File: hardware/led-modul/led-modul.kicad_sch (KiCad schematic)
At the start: 0 parts

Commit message: Hardver: LED-modul kapcsolási rajz (vázlat) + generátor
6 low-side csatorna (NTD5C648NL, 3 × UCC27524, B360B szabadonfutó, RC snubber
DNP), blokkonként SMD biztosíték, ideális dióda (LM74700-Q1 + NTMFS5C604NL)
a 20 A-es ágon, gate- és drain-LED-ek, drain → ADC, 1 mΩ sönt + INA181A2,
NTC, MC78L12, HW-ID 2. sáv. DRV_EN-lehúzás 1 kΩ (D65). ERC: 0 hiba.

Co-Authored-By: Claude Opus 5.5 <noreply@anthropic.com>
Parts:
- added C201, C202, C207, C211, C213, C215, C240, C242: 100n, Capacitor_SMD:C_0603_1608Metric, symbol Device:C
- added C203: 470µ/50V, Capacitor_THT:CP_Radial_D10.0mm_P5.00mm, symbol Device:C_Polarized
- added C204, C205, C206: 10µ/50V, Capacitor_SMD:C_1210_3225Metric, symbol Device:C
- added C208: 1µ/50V, Capacitor_SMD:C_0805_2012Metric, symbol Device:C
- added C209: 10µ/25V, Capacitor_SMD:C_1206_3216Metric, symbol Device:C
- added C210, C212, C214: 1µ/25V, Capacitor_SMD:C_0805_2012Metric, symbol Device:C
- added C221, C222, C223, C224, C225, C226: 2n2/100V, Capacitor_SMD:C_1206_3216Metric, symbol Device:C
- added C231, C232, C233, C234, C235, C236: 10n, Capacitor_SMD:C_0603_1608Metric, symbol Device:C
- added C241: 1n, Capacitor_SMD:C_0603_1608Metric, symbol Device:C
- added D201: SMBJ28A, Diode_SMD:D_SMB, symbol Device:D_Zener
- added D211, D212, D213, D214, D215, D216: B360B, Diode_SMD:D_SMB, symbol Device:D_Schottky
- added D221, D222, D223, D224, D225, D226, D231, D232, D233, D234, D235, D236: zöld, LED_SMD:LED_0603_1608Metric, symbol Device:LED
- added F201: 20A, Fuse:Fuseholder_Blade_Mini_Keystone_3568, symbol Device:Fuse
- added F202, F203, F204: 10A, Fuse:Fuse_Littelfuse-NANO2-451_453, symbol Device:Fuse
- added J201: 24V IN 20A, TerminalBlock_Phoenix:TerminalBlock_Phoenix_MKDS-3-2-5.08_1x02_P5.08mm_Horizontal, symbol Connector_Generic:Conn_01x02
- added J202: BLOKK 1, TerminalBlock_Phoenix:TerminalBlock_Phoenix_MKDS-3-3-5.08_1x03_P5.08mm_Horizontal, symbol Connector_Generic:Conn_01x03
- added J203: BLOKK 2, TerminalBlock_Phoenix:TerminalBlock_Phoenix_MKDS-3-3-5.08_1x03_P5.08mm_Horizontal, symbol Connector_Generic:Conn_01x03
- added J204: BLOKK 3, TerminalBlock_Phoenix:TerminalBlock_Phoenix_MKDS-3-3-5.08_1x03_P5.08mm_Horizontal, symbol Connector_Generic:Conn_01x03
- added Q201: NTMFS5C604NL, Package_SO:ONSemi_SO-8FL_488AA, symbol Transistor_FET:NTMFS016N06CT1G
- added Q202, Q203, Q204, Q205, Q206, Q207: NTD5C648NL, Package_TO_SOT_SMD:TO-252-2, symbol Transistor_FET:QM6006D
- added R201, R208: 10k 1%, Resistor_SMD:R_0603_1608Metric, symbol Device:R
- added R202: 3k3 1%, Resistor_SMD:R_0603_1608Metric, symbol Device:R
- added R203: 100k, Resistor_SMD:R_0603_1608Metric, symbol Device:R
- added R204, R221, R222, R223, R224, R225, R226: 10k, Resistor_SMD:R_0603_1608Metric, symbol Device:R
- added R205: 1k, Resistor_SMD:R_0603_1608Metric, symbol Device:R
- added R207: 100R, Resistor_SMD:R_0603_1608Metric, symbol Device:R
- added R209: 1m 1%, Resistor_SMD:R_Shunt_Vishay_WSK2512_6332Metric_T1.19mm, symbol Device:R_Shunt
- added R211, R212, R213, R214, R215, R216: 10R, Resistor_SMD:R_0603_1608Metric, symbol Device:R
- added R231, R232, R233, R234, R235, R236: 10R, Resistor_SMD:R_1206_3216Metric, symbol Device:R
- added R241, R242, R243, R244, R245, R246: 4k7, Resistor_SMD:R_0603_1608Metric, symbol Device:R
- added R251, R252, R253, R254, R255, R256: 10k, Resistor_SMD:R_0805_2012Metric, symbol Device:R
- added R261, R262, R263, R264, R265, R266: 470k, Resistor_SMD:R_0603_1608Metric, symbol Device:R
- added R271, R272, R273, R274, R275, R276: 56k, Resistor_SMD:R_0603_1608Metric, symbol Device:R
- added TH201: 10k B3435, Resistor_SMD:R_0603_1608Metric, symbol Device:Thermistor_NTC
- added TP201: DAC_THR, TestPoint:TestPoint_Pad_D1.5mm, symbol Connector:TestPoint
- added TP202: I_SENSE, TestPoint:TestPoint_Pad_D1.5mm, symbol Connector:TestPoint
- added U201, U202, U203: UCC27524DR, Package_SO:SOIC-8_3.9x4.9mm_P1.27mm, symbol Driver_FET:UCC27524D
- added U204: LM74700-Q1, Package_TO_SOT_SMD:SOT-23-6, symbol Power_Management:LM74700
- added U205: MC78L12ACDR2G, Package_SO:SOIC-8_3.9x4.9mm_P1.27mm, symbol Regulator_Linear:MC78L12_SO8
- added U206: INA181A2IDBVR, Package_TO_SOT_SMD:SOT-23-6, symbol Amplifier_Current:INA181
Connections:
- new net +12V: C209.1, C210.1, C211.1, C212.1, C213.1, C214.1, C215.1, U201.6 (V_{DD}), U202.6 (V_{DD}), U203.6 (V_{DD}), U205.1 (OUT)
- new net +24V_B1: D211.1 (K), D212.1 (K), F202.2, J202.1 (Pin_1), R251.1, R252.1
- new net +24V_B2: D213.1 (K), D214.1 (K), F203.2, J203.1 (Pin_1), R253.1, R254.1
- new net +24V_B3: D215.1 (K), D216.1 (K), F204.2, J204.1 (Pin_1), R255.1, R256.1
- new net +24V_F: C202.2, F201.2, Q201.1 (S), Q201.2 (S), Q201.3 (S), U204.3 (EN), U204.6 (ANODE)
- new net +24V_IN: F201.1, J201.1 (Pin_1)
- new net +24V_RAIL: C203.1, C204.1, C205.1, C206.1, C208.1, D201.1 (K), F202.1, F203.1, F204.1, Q201.5 (D), R203.1, U204.4 (CATHODE), U205.8 (IN)
- new net +3V3: C240.1, R201.1, R208.1, U206.6 (V+)
- new net CH1_D: D211.2 (A), D231.1 (K), J202.2 (Pin_2), Q202.2 (D), R231.1, R261.1
- new net CH1_G: Q202.1 (G), R211.2, R221.1
- new net CH1_GD: R211.1, R241.1, U201.7 (OUTA)
- new net CH1_PWM: U201.2 (INA)
- new net CH1_SN: C221.1, R231.2
- new net CH2_D: D212.2 (A), D232.1 (K), J202.3 (Pin_3), Q203.2 (D), R232.1, R262.1
- new net CH2_G: Q203.1 (G), R212.2, R222.1
- new net CH2_GD: R212.1, R242.1, U201.5 (OUTB)
- new net CH2_PWM: U201.4 (INB)
- new net CH2_SN: C222.1, R232.2
- new net CH3_D: D213.2 (A), D233.1 (K), J203.2 (Pin_2), Q204.2 (D), R233.1, R263.1
- new net CH3_G: Q204.1 (G), R213.2, R223.1
- new net CH3_GD: R213.1, R243.1, U202.7 (OUTA)
- new net CH3_PWM: U202.2 (INA)
- new net CH3_SN: C223.1, R233.2
- new net CH4_D: D214.2 (A), D234.1 (K), J203.3 (Pin_3), Q205.2 (D), R234.1, R264.1
- new net CH4_G: Q205.1 (G), R214.2, R224.1
- new net CH4_GD: R214.1, R244.1, U202.5 (OUTB)
- new net CH4_PWM: U202.4 (INB)
- new net CH4_SN: C224.1, R234.2
- new net CH5_D: D215.2 (A), D235.1 (K), J204.2 (Pin_2), Q206.2 (D), R235.1, R265.1
- new net CH5_G: Q206.1 (G), R215.2, R225.1
- new net CH5_GD: R215.1, R245.1, U203.7 (OUTA)
- new net CH5_PWM: U203.2 (INA)
- new net CH5_SN: C225.1, R235.2
- new net CH6_D: D216.2 (A), D236.1 (K), J204.3 (Pin_3), Q207.2 (D), R236.1, R266.1
- new net CH6_G: Q207.1 (G), R216.2, R226.1
- new net CH6_GD: R216.1, R246.1, U203.5 (OUTB)
- new net CH6_PWM: U203.4 (INB)
- new net CH6_SN: C226.1, R236.2
- new net DAC_THR: TP201.1
- new net DLED1: D231.2 (A), R251.2
- new net DLED2: D232.2 (A), R252.2
- new net DLED3: D233.2 (A), R253.2
- new net DLED4: D234.2 (A), R254.2
- new net DLED5: D235.2 (A), R255.2
- new net DLED6: D236.2 (A), R256.2
- new net DRV_EN: R205.1, U201.1 (ENA), U201.8 (ENB), U202.1 (ENA), U202.8 (ENB), U203.1 (ENA), U203.8 (ENB)
- new net DS1: C231.1, R261.2, R271.1
- new net DS2: C232.1, R262.2, R272.1
- new net DS3: C233.1, R263.2, R273.1
- new net DS4: C234.1, R264.2, R274.1
- new net DS5: C235.1, R265.2, R275.1
- new net DS6: C236.1, R266.2, R276.1
- new net GLED1: D221.2 (A), R241.2
- new net GLED2: D222.2 (A), R242.2
- new net GLED3: D223.2 (A), R243.2
- new net GLED4: D224.2 (A), R244.2
- new net GLED5: D225.2 (A), R245.2
- new net GLED6: D226.2 (A), R246.2
- new net GND: C201.2, C203.2, C204.2, C205.2, C206.2, C207.2, C208.2, C209.2, C210.2, C211.2, C212.2, C213.2, C214.2, C215.2, C231.2, C232.2, C233.2, C234.2, C235.2, C236.2, C240.2, C241.2, C242.2, D201.2 (A), D221.1 (K), D222.1 (K), D223.1 (K), D224.1 (K), D225.1 (K), D226.1 (K), J201.2 (Pin_2), R202.2, R204.2, R205.2, R209.4, R271.2, R272.2, R273.2, R274.2, R275.2, R276.2, TH201.2, U201.3 (GND), U202.3 (GND), U203.3 (GND), U204.2 (GND), U205.2 (GND), U205.3 (GND), U205.6 (GND), U205.7 (GND), U206.2 (GND), U206.5 (REF)
- new net HW_ID: C201.1, R201.2, R202.1
- new net IDEAL_GATE: Q201.4 (G), U204.5 (GATE)
- new net IDEAL_VCAP: C202.1, U204.1 (VCAP)
- new net INA_OUT: R207.1, U206.1
- new net ISNS_N: R209.3, U206.4 (-)
- new net ISNS_P: R209.2, U206.3 (+)
- new net I_SENSE: C241.1, R207.2, TP202.1
- new net NTC: C242.1, R208.2, TH201.1
- new net PGND_SH: C221.2, C222.2, C223.2, C224.2, C225.2, C226.2, Q202.3 (S), Q203.3 (S), Q204.3 (S), Q205.3 (S), Q206.3 (S), Q207.3 (S), R209.1, R221.2, R222.2, R223.2, R224.2, R225.2, R226.2
- new net V_RAIL_SENSE: C207.1, R203.2, R204.1
- no-connect marks 0 -> 10
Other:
- added sheet modulmag (../modulmag/modulmag.kicad_sch)
- note added: "1 mΩ sönt: PGND_SH (FET-source-ok) → GND, Kelvin"
- note added: "1. BETÁP (20 A): J201 → F201 20 A (mini lapos) → ideális dióda (U204 LM74700-Q1 + Q201) → +24V_RAIL"
- note added: "2. KIMENETI BLOKKOK: [+24 V, CHa, CHb] × 3, blokkonként SMD biztosíték (D65) – a szalagok közös vezetéke a +24 V (low-side, D43)"
- note added: "3. GATE-MEGHAJTÓK – 3 × UCC27524 (12 V): EN közösen a DRV_EN-en (PB12), 1 k lehúzás → bekapcsoláskor minden csatorna KI"
- note added: "4. CSATORNÁK (× 6): FET NTD5C648NL (DPAK; tartalék IRFR1205) · szabadonfutó B360B a blokk +24 V-jára · RC snubber (DNP)"
- note added: "5. ÖSSZ-ÁRAM (D47, D53)"
- note added: "6 EN-láb belső 200 k felhúzása a 12 V-ra párhuzamosan ~33 k → 1 k-val ~0,35 V (< 0,8 V); az IN-lábakon 120 k belső lehúzás is van"
- note added: "BE: ≈ V_RAIL × (1 − kitöltés); mindig ~0 V = átütött FET. A „nincs szalag” biztosan az önteszt áramméréséből (D47) látszik."
- note added: "Drain → ADC: 24 V → 2,55 V (PA0–PA3, PA5, PA6). KI: ≈ V_RAIL = szalag rajta; ≈ V_RAIL − ~2 V = nincs szalag (a drain-LED-en át, halványan dereng); ~0 V = kiolvadt blokk-biztosíték"
- note added: "HW-ID: LED-modul = 2. sáv (0,82 V)"
- note added: "INA181A2 (×50) → PA7: ADC + COMP2 → TIM1/TIM8 break"
- note added: "MODULMAG – a logikai táp a 20 A-es"
- note added: "NTC a FET-ek között (PC3)"
- note added: "V_RAIL: 24 V → 2,2 V (PC2); a VIN_SENSE-szel (PC1)"
- note added: "VÁZLAT – generálva a MODULMAG-SPEC + D43/D47/D53/D65 alapján (2026-10-14). Elrendezést rendezd; a bekötés címkékkel kész."
- note added: "együtt a kiégett F201 / hibás Q201 jelezhető"
- note added: "fordított polaritás ellen, GND-eltolódás nélkül (D65); Q201 hiányában S–D dróttal áthidalható"
- note added: "főbiztosíték ELŐTT ágazik le (D54)"
- note added: "gate-LED (driver kimenet) + drain-LED (a blokk +24 V-ja → drain) · drain → ADC osztó (D65)"
- note added: "küszöb: DAC1 (PA4); 20 A → 1,0 V"
- title: LED-modul (6 csatorna) -> LED-modul – 6 × 10 A low-side PWM (össz. 20 A), modulmag

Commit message: Hardver: mind az öt kapcsolási rajz elrendezve (vezetékes, blokkos), netlista-ellenőrzővel
Funkcionális blokkok, balról jobbra jelút, tápsín felül / GND alul; blokkon belül
vezeték, blokkok között és az IC-lábakon címke. kigen: lábpozíció, place(),
wire/junction/rail, tükrözés, 1,27 mm-es rács, olvasható mezők. gen/netcmp.py:
két netlista lábszintű összevetése – a bekötés az átrendezés előttivel azonos
(a modulmag D66-os D6/JP2-jét kivéve). ERC: 0 hiba mind az öt lapon.

Co-Authored-By: Claude Opus 5.5 <noreply@anthropic.com>
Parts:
- C203: Megjegyzés low-ESR, 105 °C; a GND-oldala a sönt ELŐTT (a sönt a FET-ár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 -> low-ESR, 105 °C; GND-oldala a sönt ELŐTT
- C204, C205, C206: Megjegyzés a FET-ek mellett, csatornapáronként egy -> a FET-ek mellett
- D201: Megjegyzés TVS a sínen – a P78E05-ös logikai ágon a modulmag D2-je véd -> TVS a sínen
- J201: Megjegyzés push-in, 2,5 mm², ≥ 20 A – helyőrző, a DIN-ház szerint; bar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 -> push-in, 2,5 mm², ≥ 20 A – helyőrző; barna = +24 V, kék = G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
- Q201: Megjegyzés onsemi 60 V, ~1,2 mΩ, SO-8FL; S = bemenet, D = sín. Nagy pa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 -> onsemi 60 V, ~1,2 mΩ, SO-8FL; S = bemenet, D = sín; nagy pa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
- TH201: Megjegyzés a FET-ek között, a NYÁK-on (D30 – harmadik védelmi réteg) -> (none)
- U204: Megjegyzés TI ideális dióda-vezérlő; EN az ANODE-ra (mindig BE) -> TI ideális dióda-vezérlő; EN az ANODE-ra
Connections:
- net CH1_G: no longer names the net of Q202.1 (G), R211.2, R221.1
- net CH1_SN: no longer names the net of C221.1, R231.2
- net CH2_G: no longer names the net of Q203.1 (G), R212.2, R222.1
- net CH2_SN: no longer names the net of C222.1, R232.2
- net CH3_G: no longer names the net of Q204.1 (G), R213.2, R223.1
- net CH3_SN: no longer names the net of C223.1, R233.2
- net CH4_G: no longer names the net of Q205.1 (G), R214.2, R224.1
- net CH4_SN: no longer names the net of C224.1, R234.2
- net CH5_G: no longer names the net of Q206.1 (G), R215.2, R225.1
- net CH5_SN: no longer names the net of C225.1, R235.2
- net CH6_G: no longer names the net of Q207.1 (G), R216.2, R226.1
- net CH6_SN: no longer names the net of C226.1, R236.2
- net DLED1: no longer names the net of D231.2 (A), R251.2
- net DLED2: no longer names the net of D232.2 (A), R252.2
- net DLED3: no longer names the net of D233.2 (A), R253.2
- net DLED4: no longer names the net of D234.2 (A), R254.2
- net DLED5: no longer names the net of D235.2 (A), R255.2
- net DLED6: no longer names the net of D236.2 (A), R256.2
- net GLED1: no longer names the net of D221.2 (A), R241.2
- net GLED2: no longer names the net of D222.2 (A), R242.2
- net GLED3: no longer names the net of D223.2 (A), R243.2
- net GLED4: no longer names the net of D224.2 (A), R244.2
- net GLED5: no longer names the net of D225.2 (A), R245.2
- net GLED6: no longer names the net of D226.2 (A), R246.2
- net IDEAL_GATE: no longer names the net of Q201.4 (G), U204.5 (GATE)
- net IDEAL_VCAP: no longer names the net of C202.1, U204.1 (VCAP)
- net INA_OUT: no longer names the net of R207.1, U206.1
- net ISNS_N: no longer names the net of R209.3, U206.4 (-)
- net ISNS_P: no longer names the net of R209.2, U206.3 (+)
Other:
- note added: "(ADC + COMP2 → TIM1/TIM8 break); a küszöb a DAC1-ről (PA4); 20 A → 1,0 V"
- note added: "1. BETÁP (20 A): J201 → F201 20 A → ideális dióda (U204 LM74700-Q1 + Q201) → +24V_RAIL – fordított polaritás ellen, GND-eltolódás nélkül (D65)"
- note added: "2. GATE-MEGHAJTÓK – 3 × UCC27524 (12 V): EN közösen a DRV_EN-en (PB12), 1 k lehúzás → bekapcsoláskor minden csatorna KI"
- note added: "3. CSATORNÁK (× 6): FET NTD5C648NL (DPAK; tartalék IRFR1205) · szabadonfutó B360B a blokk +24 V-jára · RC snubber (DNP) · gate-LED + drain-LED · drain → ADC osztó"
- note added: "4. ÖSSZ-ÁRAM (D47, D53): 1 mΩ sönt a FET-ek közös source-ága (PGND_SH) és a GND között, Kelvin → INA181A2 (×50) → PA7"
- note added: "CH1"
- note added: "CH2"
- note added: "CH3"
- note added: "CH4"
- note added: "CH5"
- note added: "CH6"
- note added: "Drain → ADC: 24 V → 2,55 V. KI: ≈ V_RAIL = szalag rajta; ≈ V_RAIL − ~2 V = nincs szalag (a drain-LED-en át); ~0 V = kiolvadt blokk-biztosíték. BE: ≈ V_RAIL × (1 − kitöltés); mindig ~0 V = átütött FET"
- note added: "Generálva (hardware/gen/led-modul.py) – D43/D47/D53/D65 alapján; kézi szerkesztés helyett a generátort módosítsd."
- note added: "NTC a FET-ek között (PC3) – D30, harmadik védelmi réteg"
- note added: "Q201 hiányában a S–D padek vastag dróttal áthidalhatók"
- note added: "V_RAIL → PC2"
- note added: "pufferek: a GND-oldaluk a sönt előtt"
- note removed: "1 mΩ sönt: PGND_SH (FET-source-ok) → GND, Kelvin"
- note removed: "1. BETÁP (20 A): J201 → F201 20 A (mini lapos) → ideális dióda (U204 LM74700-Q1 + Q201) → +24V_RAIL"
- note removed: "2. KIMENETI BLOKKOK: [+24 V, CHa, CHb] × 3, blokkonként SMD biztosíték (D65) – a szalagok közös vezetéke a +24 V (low-side, D43)"
- note removed: "3. GATE-MEGHAJTÓK – 3 × UCC27524 (12 V): EN közösen a DRV_EN-en (PB12), 1 k lehúzás → bekapcsoláskor minden csatorna KI"
- note removed: "4. CSATORNÁK (× 6): FET NTD5C648NL (DPAK; tartalék IRFR1205) · szabadonfutó B360B a blokk +24 V-jára · RC snubber (DNP)"
- note removed: "5. ÖSSZ-ÁRAM (D47, D53)"
- note removed: "BE: ≈ V_RAIL × (1 − kitöltés); mindig ~0 V = átütött FET. A „nincs szalag” biztosan az önteszt áramméréséből (D47) látszik."
- note removed: "Drain → ADC: 24 V → 2,55 V (PA0–PA3, PA5, PA6). KI: ≈ V_RAIL = szalag rajta; ≈ V_RAIL − ~2 V = nincs szalag (a drain-LED-en át, halványan dereng); ~0 V = kiolvadt blokk-biztosíték"
- note removed: "INA181A2 (×50) → PA7: ADC + COMP2 → TIM1/TIM8 break"
- note removed: "NTC a FET-ek között (PC3)"
- note removed: "V_RAIL: 24 V → 2,2 V (PC2); a VIN_SENSE-szel (PC1)"
- note removed: "VÁZLAT – generálva a MODULMAG-SPEC + D43/D47/D53/D65 alapján (2026-10-14). Elrendezést rendezd; a bekötés címkékkel kész."
- note removed: "együtt a kiégett F201 / hibás Q201 jelezhető"
- note removed: "fordított polaritás ellen, GND-eltolódás nélkül (D65); Q201 hiányában S–D dróttal áthidalható"
- note removed: "gate-LED (driver kimenet) + drain-LED (a blokk +24 V-ja → drain) · drain → ADC osztó (D65)"
- note removed: "küszöb: DAC1 (PA4); 20 A → 1,0 V"

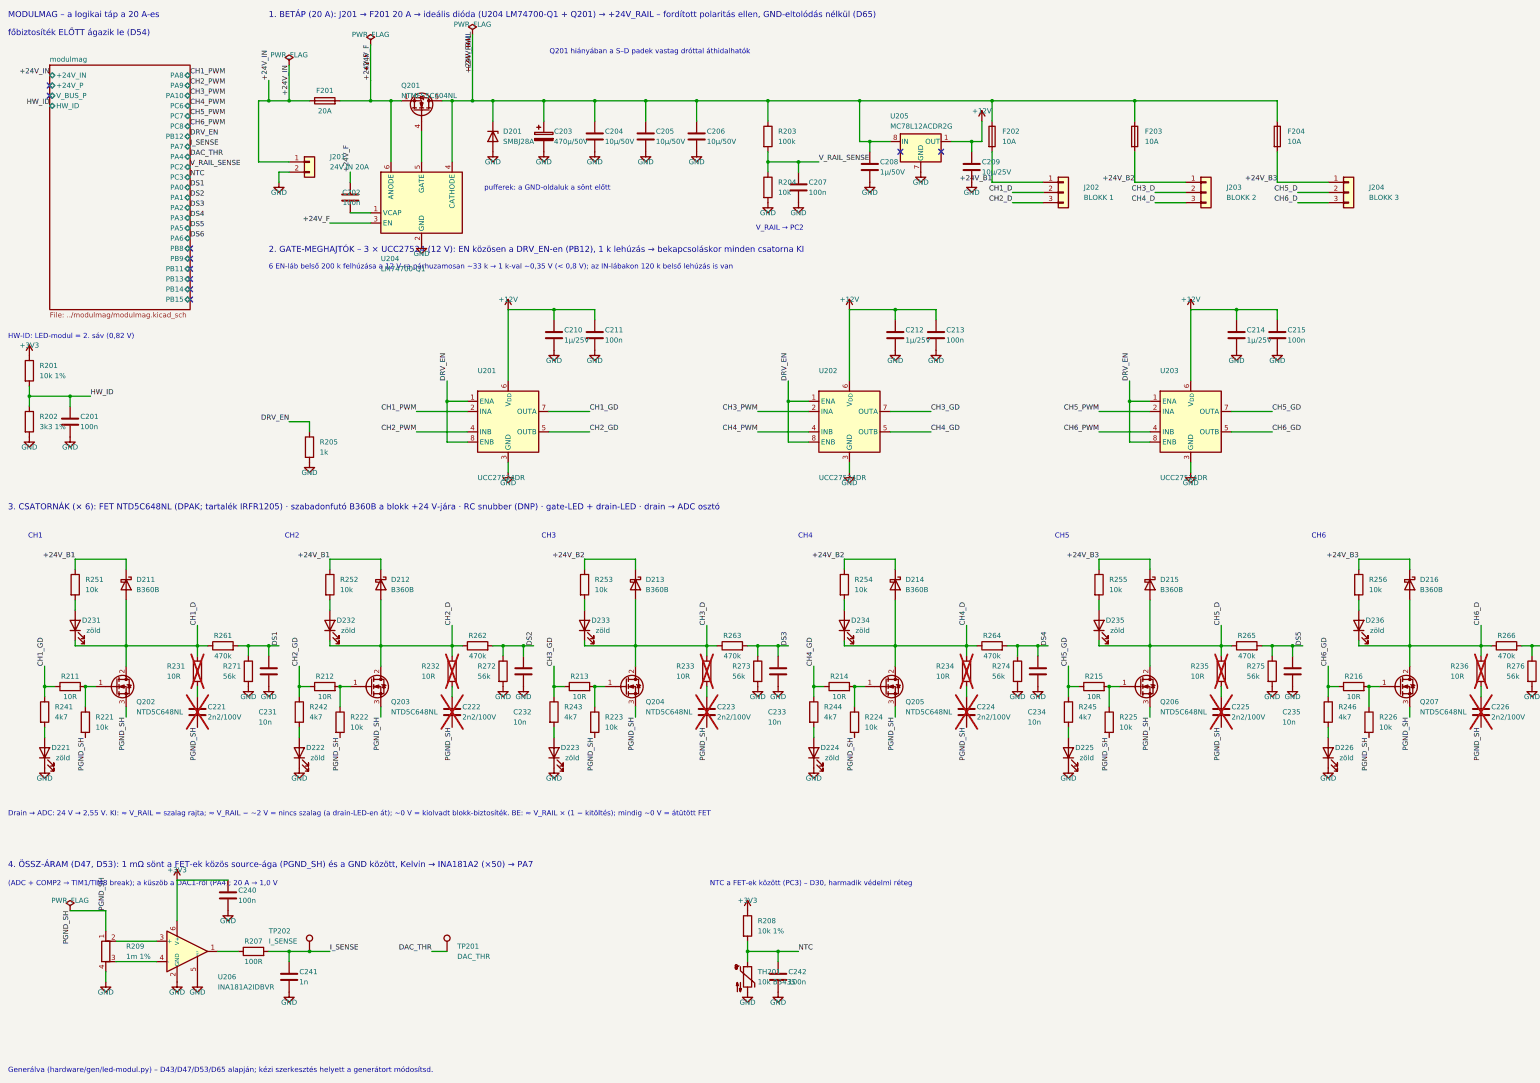
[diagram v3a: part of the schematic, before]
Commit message: Hardver: átnézés (C320 javítva), LoRa-előkészítés (D68), bővítők (D69), R6/R7 = 0 Ω (D70)
- bemeneti modul: a HDC3020 hidegítője C330 lett (a C320 kétszer szerepelt);
  a generátor mostantól hibát dob duplikált jelölésre
- vezérlő: E22-900M22S LoRa + u.FL + 74LVC1G04, minden DNP; J8 bővítő (GPIO5),
  7 mérőpont; spec szerinti DNP-k (USB C, 1 MΩ, PMODE, CAN-fojtó + áthidalók);
  saját footprint az LMR36015-höz (RNX) és az E22-höz
- modulmag: HW_REV osztó (PB0), DNP J4 2 × 5 bővítő; relé: DNP SCT-013 → PA0
- mind az öt lap vizuálisan rendbe téve; R6/R7 = 0 Ω
- specek és döntésnapló frissítve (D68–D70)

Co-Authored-By: Claude Opus 5.5 <noreply@anthropic.com>
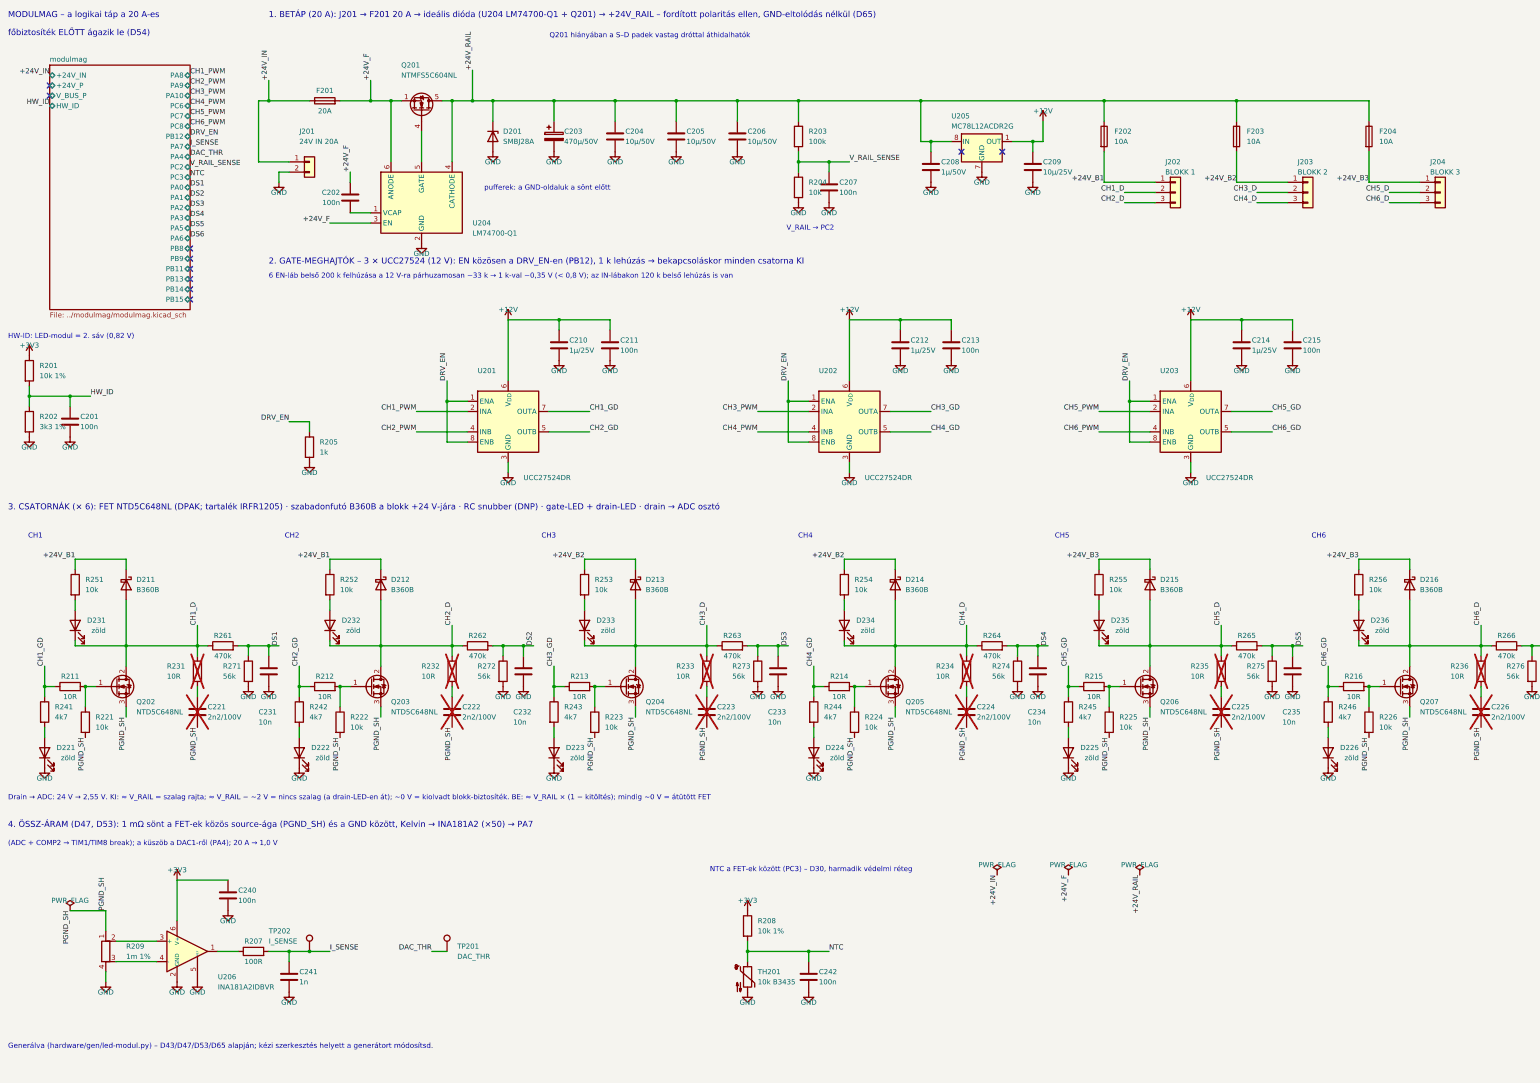
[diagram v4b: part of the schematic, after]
